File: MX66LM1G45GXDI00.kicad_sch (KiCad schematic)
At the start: 11 parts, among them U2 MX66LM1G45GXDI00

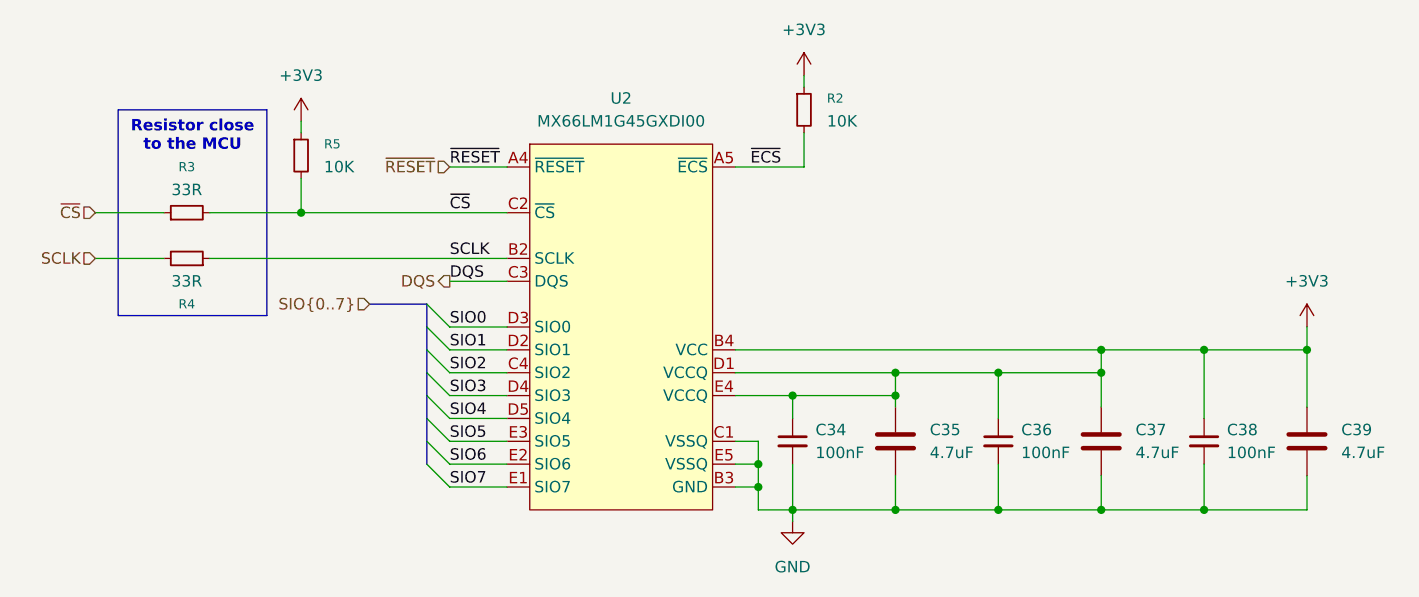
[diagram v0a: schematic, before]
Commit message: Added Battery Fuel Gauge, Battery Charger and 5V boost voltage
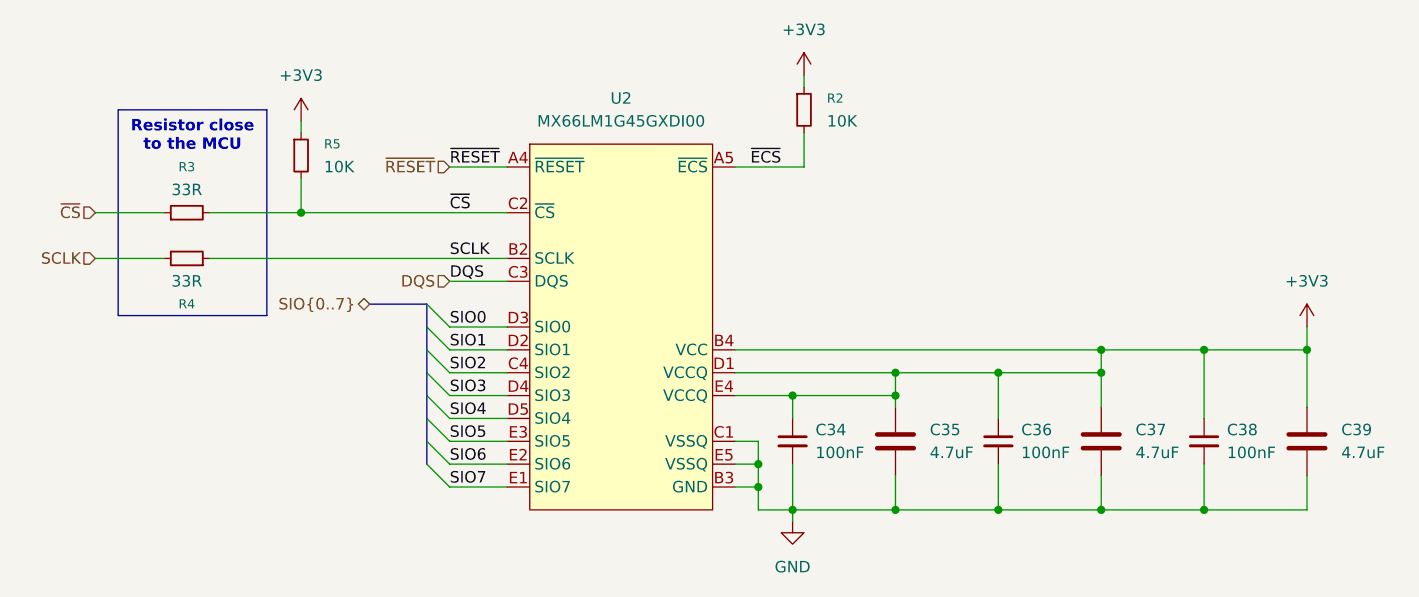
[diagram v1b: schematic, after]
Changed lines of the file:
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@@
 	)
 	(hierarchical_label "SIO{0..7}"
-		(shape input)
+		(shape bidirectional)
 		(at 111.76 105.41 180)
 		(effects
@@
 	)
 	(hierarchical_label "DQS"
-		(shape output)
+		(shape input)
 		(at 120.65 102.87 180)
 		(effects

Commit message: layouting component to PCB
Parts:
- C34, C36, C38: footprint (none) -> Capacitor_SMD:C_0402_1005Metric
- C35, C37, C39: footprint (none) -> Capacitor_SMD:C_0603_1608Metric
- R2, R3, R4, R5: footprint (none) -> Resistor_SMD:R_0402_1005Metric
- U2: footprint (none) -> MX66LM1G45GXDI00:CSP24BGA_MAC-M
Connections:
- net SCLK: no longer R4.1, U2.B2 (SCLK)
- net ~{CS}: no longer R3.2, R5.2, U2.C2 (~{CS})
- new net: R3.2, R5.2, U2.C2 (~{CS})
- new net: R4.1, U2.B2 (SCLK)
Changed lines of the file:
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@@
-		)
-	)
-	(label "SCLK"
-		(at 120.65 100.33 0)
-		(effects
-			(font
-				(size 1.27 1.27)
-			)
-			(justify left bottom)
 		)
 	)
@@
 	(label "SIO7"
 		(at 120.65 125.73 0)
-		(effects
-			(font
-				(size 1.27 1.27)
-			)
-			(justify left bottom)
-		)
-	)
-	(label "~{CS}"
-		(at 120.65 95.25 0)
 		(effects
 			(font
@@
 			)
 		)
-		(property "Footprint" ""
+		(property "Footprint" "Capacitor_SMD:C_0603_1608Metric"
 			(at 216.8652 124.46 0)
 			(effects
@@
 			)
 		)
-		(property "Footprint" ""
+		(property "Footprint" "Capacitor_SMD:C_0402_1005Metric"
 			(at 181.61 120.65 0)
 			(effects
@@
 			)
 		)
-		(property "Footprint" ""
+		(property "Footprint" "Resistor_SMD:R_0402_1005Metric"
 			(at 104.14 88.9 0)
 			(effects
@@
 			)
 		)
-		(property "Footprint" ""
+		(property "Footprint" "Capacitor_SMD:C_0402_1005Metric"
 			(at 158.75 120.65 0)
 			(effects
@@
 			)
 		)
-		(property "Footprint" ""
+		(property "Footprint" "Capacitor_SMD:C_0603_1608Metric"
 			(at 194.0052 124.46 0)
 			(effects
@@
 			)
 		)
-		(property "Footprint" ""
+		(property "Footprint" "Capacitor_SMD:C_0603_1608Metric"
 			(at 171.1452 124.46 0)
 			(effects
@@
 			)
 		)
-		(property "Footprint" ""
+		(property "Footprint" "Capacitor_SMD:C_0402_1005Metric"
 			(at 204.47 120.65 0)
 			(effects
@@
 			)
 		)
-		(property "Footprint" ""
+		(property "Footprint" "Resistor_SMD:R_0402_1005Metric"
 			(at 160.02 83.82 0)
 			(effects
@@
 			)
 		)
-		(property "Footprint" ""
+		(property "Footprint" "Resistor_SMD:R_0402_1005Metric"
 			(at 91.44 100.33 0)
 			(effects
@@
 			)
 		)
-		(property "Footprint" ""
+		(property "Footprint" "MX66LM1G45GXDI00:CSP24BGA_MAC-M"
 			(at 129.54 87.63 0)
 			(effects
@@
 			)
 		)
-		(property "Footprint" ""
+		(property "Footprint" "Resistor_SMD:R_0402_1005Metric"
 			(at 91.44 95.25 0)
 			(effects

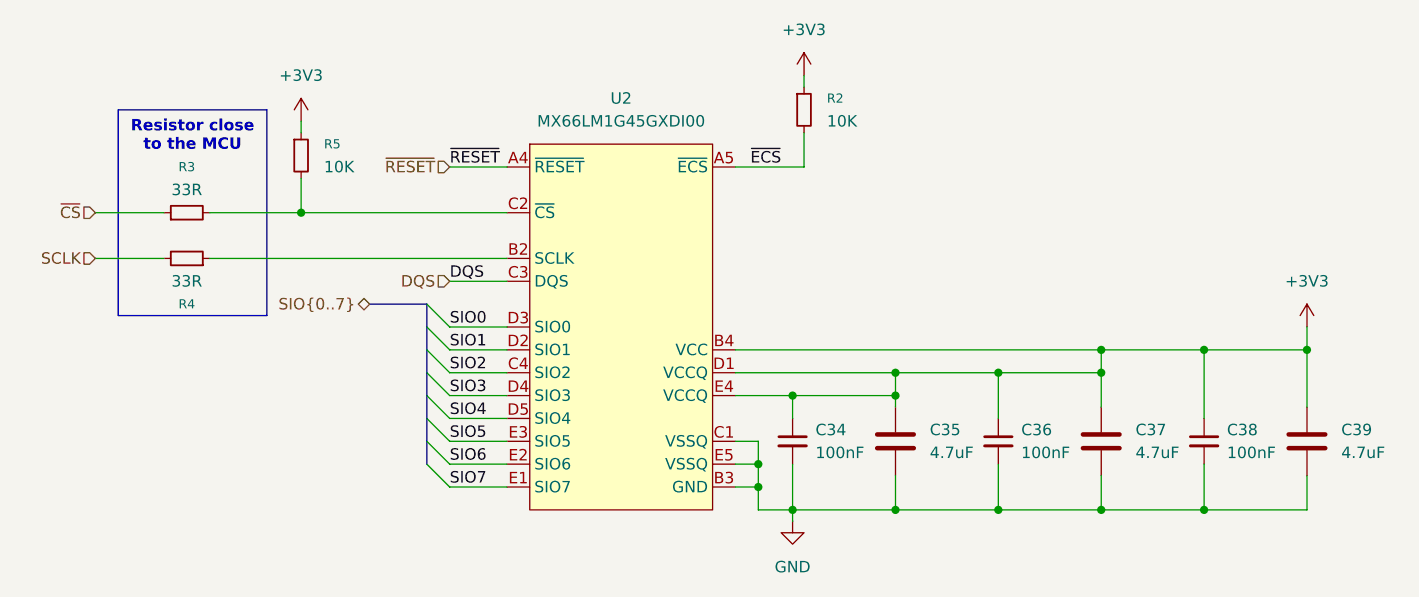
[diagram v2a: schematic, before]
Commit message: Add connection from OSPI Flash and LCD to MCU
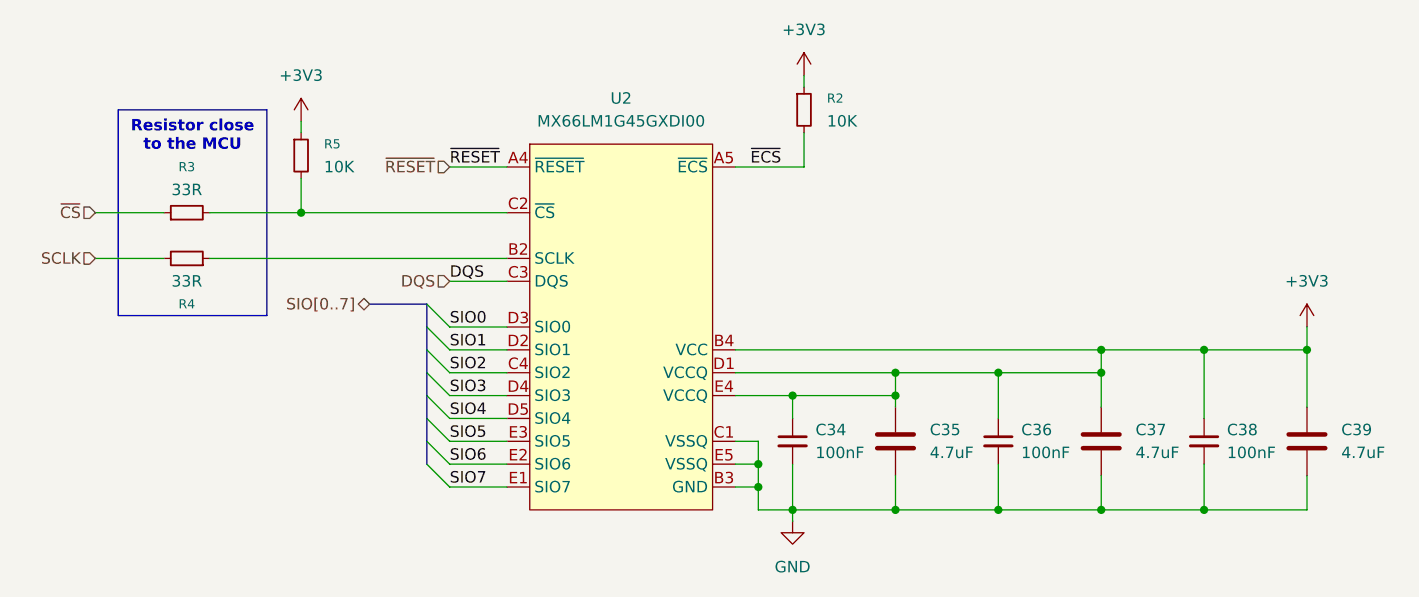
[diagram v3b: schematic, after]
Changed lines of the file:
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@@
 		)
 	)
-	(hierarchical_label "SIO{0..7}"
+	(hierarchical_label "SIO[0..7]"
 		(shape bidirectional)
 		(at 111.76 105.41 180)

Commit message: Change bypass capacitor to 0201
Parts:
- C34, C36, C38: footprint Capacitor_SMD:C_0402_1005Metric -> Capacitor_SMD:C_0201_0603Metric
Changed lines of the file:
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@@
 			)
 		)
-		(property "Footprint" "Capacitor_SMD:C_0402_1005Metric"
+		(property "Footprint" "Capacitor_SMD:C_0201_0603Metric"
 			(at 181.61 120.65 0)
 			(effects
@@
 			)
 		)
-		(property "Footprint" "Capacitor_SMD:C_0402_1005Metric"
+		(property "Footprint" "Capacitor_SMD:C_0201_0603Metric"
 			(at 158.75 120.65 0)
 			(effects
@@
 			)
 		)
-		(property "Footprint" "Capacitor_SMD:C_0402_1005Metric"
+		(property "Footprint" "Capacitor_SMD:C_0201_0603Metric"
 			(at 204.47 120.65 0)
 			(effects
